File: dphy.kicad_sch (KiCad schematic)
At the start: 5 parts, among them J1901 FFC-22p-P0.5mm, U1901 RCLAMP0524P, U1902 RCLAMP0524P, U1903 RCLAMP0524P, U1904 RCLAMP0524P

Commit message: Add comments about diff pair polarity
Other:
- note added: "DSI diff pair polarity MUST be maintained!"
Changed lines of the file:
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@@
 		(comment 3 "HALPI2 is licensed under CERN-OHL-S v2.")
+	)
+	(text "DSI diff pair polarity\nMUST be maintained!"
+		(exclude_from_sim no)
+		(at 201.676 51.562 0)
+		(effects
+			(font
+				(size 1.27 1.27)
+			)
+			(justify left)
+		)
 	)
 	(junction

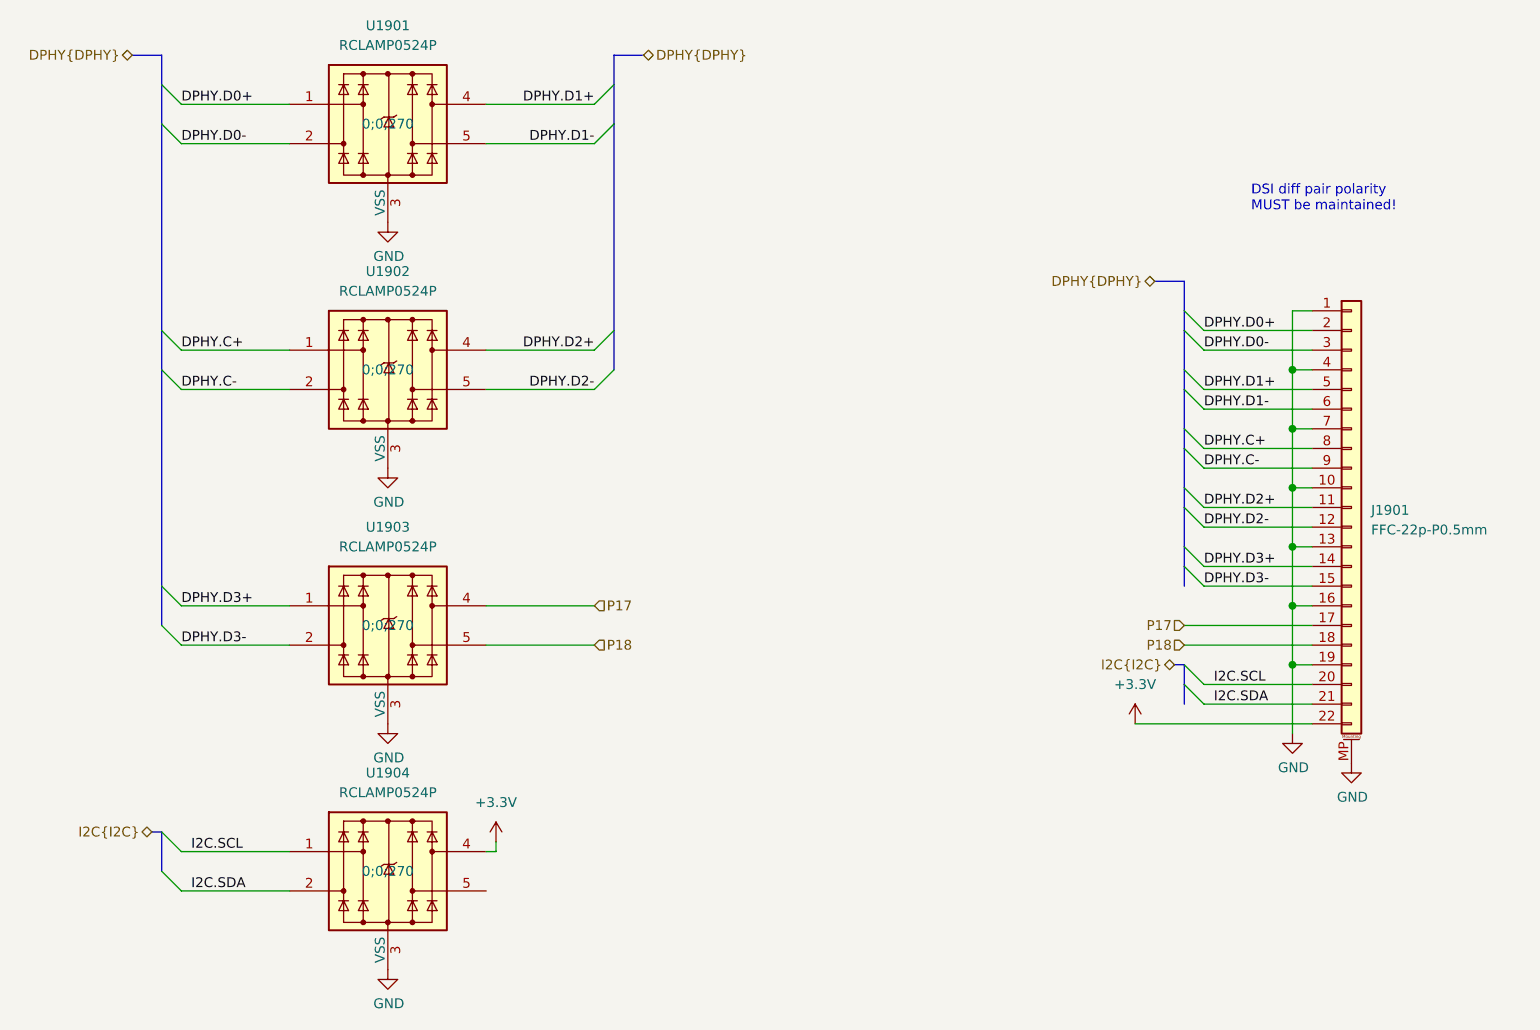
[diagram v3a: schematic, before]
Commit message: Fix DPHY pinout
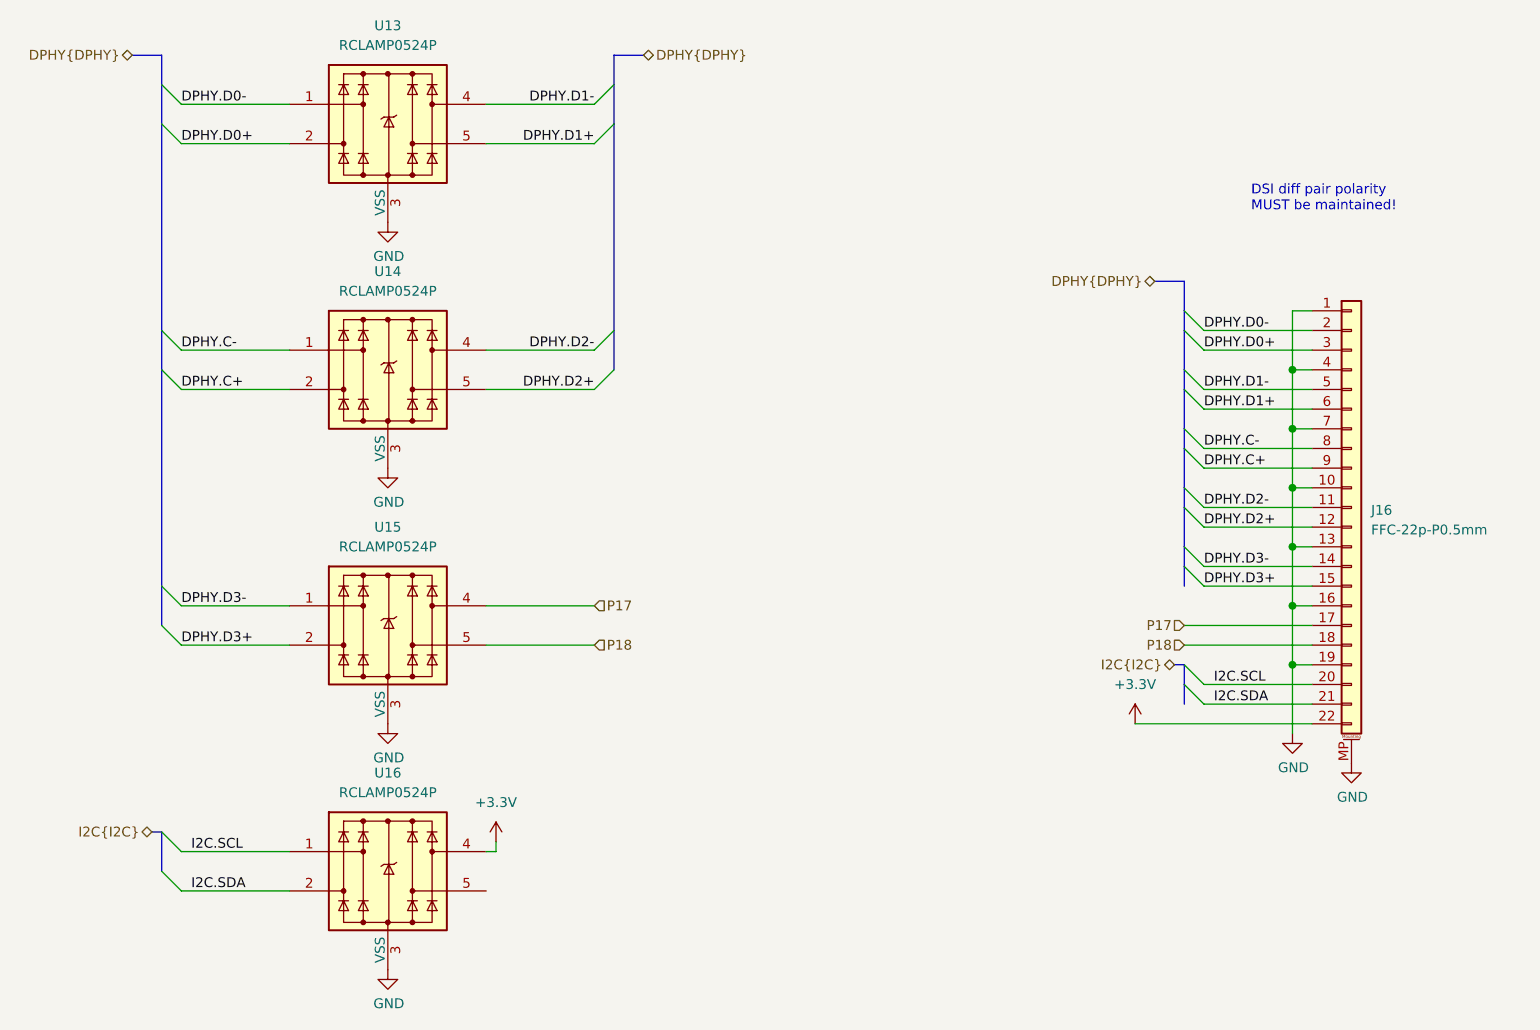
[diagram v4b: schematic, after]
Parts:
- J16: renamed from J1901; footprint Hatlabs:FFC_HDGC_0.5K-A-22PB_1x22-1SV_P0.5mm_Vertical -> HL_Connector:FFC_1x22_JUSHUO_AFC11-S22ICC-00_P0.5mm_Vertical; LCSC C2914146 -> C11074
- renumbered U1901 to U13, U1902 to U14, U1903 to U15, U1904 to U16
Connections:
- net DPHY.C+: now also J16.9 (Pin_9), U14.2, U14.9; no longer J16.8 (Pin_8), U14.1, U14.10
- net DPHY.C-: now also J16.8 (Pin_8), U14.1, U14.10; no longer J16.9 (Pin_9), U14.2, U14.9
- net DPHY.D0+: now also J16.3 (Pin_3), U13.2, U13.9; no longer J16.2 (Pin_2), U13.1, U13.10
- net DPHY.D0-: now also J16.2 (Pin_2), U13.1, U13.10; no longer J16.3 (Pin_3), U13.2, U13.9
- net DPHY.D1+: now also J16.6 (Pin_6), U13.5, U13.6; no longer J16.5 (Pin_5), U13.4, U13.7
- net DPHY.D1-: now also J16.5 (Pin_5), U13.4, U13.7; no longer J16.6 (Pin_6), U13.5, U13.6
- net DPHY.D2+: now also J16.12 (Pin_12), U14.5, U14.6; no longer J16.11 (Pin_11), U14.4, U14.7
- net DPHY.D2-: now also J16.11 (Pin_11), U14.4, U14.7; no longer J16.12 (Pin_12), U14.5, U14.6
- net DPHY.D3+: now also J16.15 (Pin_15), U15.2, U15.9; no longer J16.14 (Pin_14), U15.1, U15.10
- net DPHY.D3-: now also J16.14 (Pin_14), U15.1, U15.10; no longer J16.15 (Pin_15), U15.2, U15.9

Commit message: Reannotate the board
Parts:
- renumbered J16 to J15, U13 to U12, U14 to U13, U15 to U14, U16 to U15
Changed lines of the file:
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@@
 		(on_board yes)
 		(dnp no)
-		(property "Reference" "#PWR0117"
+		(property "Reference" "#PWR0116"
 			(at 207.01 127 0)
 			(effects
@@
 			(project "HALPI2"
 				(path "/abc482bd-3f17-4d35-80db-1da3dcdb5c27/851e7ce4-d5b0-47f7-ace9-4a347f172348/10568cce-38f9-4351-82fd-0cb3bf8ca49d"
-					(reference "#PWR0117")
-					(unit 1)
-				)
-				(path "/abc482bd-3f17-4d35-80db-1da3dcdb5c27/851e7ce4-d5b0-47f7-ace9-4a347f172348/d4876730-9038-4f8b-92bc-bcbb3a62ccf0"
-					(reference "#PWR0125")
+					(reference "#PWR0116")
+					(unit 1)
+				)
+				(path "/abc482bd-3f17-4d35-80db-1da3dcdb5c27/851e7ce4-d5b0-47f7-ace9-4a347f172348/d4876730-9038-4f8b-92bc-bcbb3a62ccf0"
+					(reference "#PWR0124")
 					(unit 1)
 				)
@@
 		(on_board yes)
 		(dnp no)
-		(property "Reference" "#PWR0112"
+		(property "Reference" "#PWR0111"
 			(at 90.17 92.71 0)
 			(effects
@@
 			(project "HALPI2"
 				(path "/abc482bd-3f17-4d35-80db-1da3dcdb5c27/851e7ce4-d5b0-47f7-ace9-4a347f172348/10568cce-38f9-4351-82fd-0cb3bf8ca49d"
-					(reference "#PWR0112")
-					(unit 1)
-				)
-				(path "/abc482bd-3f17-4d35-80db-1da3dcdb5c27/851e7ce4-d5b0-47f7-ace9-4a347f172348/d4876730-9038-4f8b-92bc-bcbb3a62ccf0"
-					(reference "#PWR0120")
+					(reference "#PWR0111")
+					(unit 1)
+				)
+				(path "/abc482bd-3f17-4d35-80db-1da3dcdb5c27/851e7ce4-d5b0-47f7-ace9-4a347f172348/d4876730-9038-4f8b-92bc-bcbb3a62ccf0"
+					(reference "#PWR0119")
 					(unit 1)
 				)
@@
 		(on_board yes)
 		(dnp no)
-		(property "Reference" "#PWR0111"
+		(property "Reference" "#PWR0110"
 			(at 90.17 60.96 0)
 			(effects
@@
 			(project "HALPI2"
 				(path "/abc482bd-3f17-4d35-80db-1da3dcdb5c27/851e7ce4-d5b0-47f7-ace9-4a347f172348/10568cce-38f9-4351-82fd-0cb3bf8ca49d"
-					(reference "#PWR0111")
-					(unit 1)
-				)
-				(path "/abc482bd-3f17-4d35-80db-1da3dcdb5c27/851e7ce4-d5b0-47f7-ace9-4a347f172348/d4876730-9038-4f8b-92bc-bcbb3a62ccf0"
-					(reference "#PWR0119")
+					(reference "#PWR0110")
+					(unit 1)
+				)
+				(path "/abc482bd-3f17-4d35-80db-1da3dcdb5c27/851e7ce4-d5b0-47f7-ace9-4a347f172348/d4876730-9038-4f8b-92bc-bcbb3a62ccf0"
+					(reference "#PWR0118")
 					(unit 1)
 				)
@@
 		(on_board yes)
 		(dnp no)
-		(property "Reference" "U16"
+		(property "Reference" "U15"
 			(at 90.17 125.73 0)
 			(effects
@@
 			(project "HALPI2"
 				(path "/abc482bd-3f17-4d35-80db-1da3dcdb5c27/851e7ce4-d5b0-47f7-ace9-4a347f172348/10568cce-38f9-4351-82fd-0cb3bf8ca49d"
-					(reference "U16")
-					(unit 1)
-				)
-				(path "/abc482bd-3f17-4d35-80db-1da3dcdb5c27/851e7ce4-d5b0-47f7-ace9-4a347f172348/d4876730-9038-4f8b-92bc-bcbb3a62ccf0"
-					(reference "U20")
+					(reference "U15")
+					(unit 1)
+				)
+				(path "/abc482bd-3f17-4d35-80db-1da3dcdb5c27/851e7ce4-d5b0-47f7-ace9-4a347f172348/d4876730-9038-4f8b-92bc-bcbb3a62ccf0"
+					(reference "U19")
 					(unit 1)
 				)
@@
 		(dnp no)
 		(fields_autoplaced yes)
-		(property "Reference" "#PWR0115"
+		(property "Reference" "#PWR0114"
 			(at 104.14 138.43 0)
 			(effects
@@
 			(project "HALPI2"
 				(path "/abc482bd-3f17-4d35-80db-1da3dcdb5c27/851e7ce4-d5b0-47f7-ace9-4a347f172348/10568cce-38f9-4351-82fd-0cb3bf8ca49d"
-					(reference "#PWR0115")
-					(unit 1)
-				)
-				(path "/abc482bd-3f17-4d35-80db-1da3dcdb5c27/851e7ce4-d5b0-47f7-ace9-4a347f172348/d4876730-9038-4f8b-92bc-bcbb3a62ccf0"
-					(reference "#PWR0123")
+					(reference "#PWR0114")
+					(unit 1)
+				)
+				(path "/abc482bd-3f17-4d35-80db-1da3dcdb5c27/851e7ce4-d5b0-47f7-ace9-4a347f172348/d4876730-9038-4f8b-92bc-bcbb3a62ccf0"
+					(reference "#PWR0122")
 					(unit 1)
 				)
@@
 		(on_board yes)
 		(dnp no)
-		(property "Reference" "U14"
+		(property "Reference" "U13"
 			(at 90.17 60.96 0)
 			(effects
@@
 			(project "HALPI2"
 				(path "/abc482bd-3f17-4d35-80db-1da3dcdb5c27/851e7ce4-d5b0-47f7-ace9-4a347f172348/10568cce-38f9-4351-82fd-0cb3bf8ca49d"
-					(reference "U14")
-					(unit 1)
-				)
-				(path "/abc482bd-3f17-4d35-80db-1da3dcdb5c27/851e7ce4-d5b0-47f7-ace9-4a347f172348/d4876730-9038-4f8b-92bc-bcbb3a62ccf0"
-					(reference "U18")
+					(reference "U13")
+					(unit 1)
+				)
+				(path "/abc482bd-3f17-4d35-80db-1da3dcdb5c27/851e7ce4-d5b0-47f7-ace9-4a347f172348/d4876730-9038-4f8b-92bc-bcbb3a62ccf0"
+					(reference "U17")
 					(unit 1)
 				)
@@
 		(on_board yes)
 		(dnp no)
-		(property "Reference" "#PWR0113"
+		(property "Reference" "#PWR0112"
 			(at 90.17 125.73 0)
 			(effects
@@
 			(project "HALPI2"
 				(path "/abc482bd-3f17-4d35-80db-1da3dcdb5c27/851e7ce4-d5b0-47f7-ace9-4a347f172348/10568cce-38f9-4351-82fd-0cb3bf8ca49d"
-					(reference "#PWR0113")
-					(unit 1)
-				)
-				(path "/abc482bd-3f17-4d35-80db-1da3dcdb5c27/851e7ce4-d5b0-47f7-ace9-4a347f172348/d4876730-9038-4f8b-92bc-bcbb3a62ccf0"
-					(reference "#PWR0121")
+					(reference "#PWR0112")
+					(unit 1)
+				)
+				(path "/abc482bd-3f17-4d35-80db-1da3dcdb5c27/851e7ce4-d5b0-47f7-ace9-4a347f172348/d4876730-9038-4f8b-92bc-bcbb3a62ccf0"
+					(reference "#PWR0120")
 					(unit 1)
 				)
@@
 		(on_board yes)
 		(dnp no)
-		(property "Reference" "#PWR0114"
+		(property "Reference" "#PWR0113"
 			(at 90.17 157.48 0)
 			(effects
@@
 			(project "HALPI2"
 				(path "/abc482bd-3f17-4d35-80db-1da3dcdb5c27/851e7ce4-d5b0-47f7-ace9-4a347f172348/10568cce-38f9-4351-82fd-0cb3bf8ca49d"
-					(reference "#PWR0114")
-					(unit 1)
-				)
-				(path "/abc482bd-3f17-4d35-80db-1da3dcdb5c27/851e7ce4-d5b0-47f7-ace9-4a347f172348/d4876730-9038-4f8b-92bc-bcbb3a62ccf0"
-					(reference "#PWR0122")
+					(reference "#PWR0113")
+					(unit 1)
+				)
+				(path "/abc482bd-3f17-4d35-80db-1da3dcdb5c27/851e7ce4-d5b0-47f7-ace9-4a347f172348/d4876730-9038-4f8b-92bc-bcbb3a62ccf0"
+					(reference "#PWR0121")
 					(unit 1)
 				)
@@
 		(on_board yes)
 		(dnp no)
-		(property "Reference" "U13"
+		(property "Reference" "U12"
 			(at 90.17 29.21 0)
 			(effects
@@
 			(project "HALPI2"
 				(path "/abc482bd-3f17-4d35-80db-1da3dcdb5c27/851e7ce4-d5b0-47f7-ace9-4a347f172348/10568cce-38f9-4351-82fd-0cb3bf8ca49d"
-					(reference "U13")
-					(unit 1)
-				)
-				(path "/abc482bd-3f17-4d35-80db-1da3dcdb5c27/851e7ce4-d5b0-47f7-ace9-4a347f172348/d4876730-9038-4f8b-92bc-bcbb3a62ccf0"
-					(reference "U17")
+					(reference "U12")
+					(unit 1)
+				)
+				(path "/abc482bd-3f17-4d35-80db-1da3dcdb5c27/851e7ce4-d5b0-47f7-ace9-4a347f172348/d4876730-9038-4f8b-92bc-bcbb3a62ccf0"
+					(reference "U16")
 					(unit 1)
 				)
@@
 		(on_board yes)
 		(dnp no)
-		(property "Reference" "#PWR0118"
+		(property "Reference" "#PWR0117"
 			(at 214.63 130.81 0)
 			(effects
@@
 			(project "HALPI2"
 				(path "/abc482bd-3f17-4d35-80db-1da3dcdb5c27/851e7ce4-d5b0-47f7-ace9-4a347f172348/10568cce-38f9-4351-82fd-0cb3bf8ca49d"
-					(reference "#PWR0118")
-					(unit 1)
-				)
-				(path "/abc482bd-3f17-4d35-80db-1da3dcdb5c27/851e7ce4-d5b0-47f7-ace9-4a347f172348/d4876730-9038-4f8b-92bc-bcbb3a62ccf0"
-					(reference "#PWR0126")
+					(reference "#PWR0117")
+					(unit 1)
+				)
+				(path "/abc482bd-3f17-4d35-80db-1da3dcdb5c27/851e7ce4-d5b0-47f7-ace9-4a347f172348/d4876730-9038-4f8b-92bc-bcbb3a62ccf0"
+					(reference "#PWR0125")
 					(unit 1)
 				)
@@
 		(dnp no)
 		(fields_autoplaced yes)
-		(property "Reference" "J16"
+		(property "Reference" "J15"
 			(at 217.17 91.7955 0)
 			(effects
@@
 				)
 				(path "/abc482bd-3f17-4d35-80db-1da3dcdb5c27/851e7ce4-d5b0-47f7-ace9-4a347f172348/10568cce-38f9-4351-82fd-0cb3bf8ca49d"
+					(reference "J15")
+					(unit 1)
+				)
+				(path "/abc482bd-3f17-4d35-80db-1da3dcdb5c27/851e7ce4-d5b0-47f7-ace9-4a347f172348/d4876730-9038-4f8b-92bc-bcbb3a62ccf0"
 					(reference "J16")
-					(unit 1)
-				)
-				(path "/abc482bd-3f17-4d35-80db-1da3dcdb5c27/851e7ce4-d5b0-47f7-ace9-4a347f172348/d4876730-9038-4f8b-92bc-bcbb3a62ccf0"
-					(reference "J17")
 					(unit 1)
 				)
@@
 		(on_board yes)
 		(dnp no)
-		(property "Reference" "U15"
+		(property "Reference" "U14"
 			(at 90.17 93.98 0)
 			(effects
@@
 			(project "HALPI2"
 				(path "/abc482bd-3f17-4d35-80db-1da3dcdb5c27/851e7ce4-d5b0-47f7-ace9-4a347f172348/10568cce-38f9-4351-82fd-0cb3bf8ca49d"
-					(reference "U15")
-					(unit 1)
-				)
-				(path "/abc482bd-3f17-4d35-80db-1da3dcdb5c27/851e7ce4-d5b0-47f7-ace9-4a347f172348/d4876730-9038-4f8b-92bc-bcbb3a62ccf0"
-					(reference "U19")
+					(reference "U14")
+					(unit 1)
+				)
+				(path "/abc482bd-3f17-4d35-80db-1da3dcdb5c27/851e7ce4-d5b0-47f7-ace9-4a347f172348/d4876730-9038-4f8b-92bc-bcbb3a62ccf0"
+					(reference "U18")
 					(unit 1)
 				)
@@
 		(dnp no)
 		(fields_autoplaced yes)
-		(property "Reference" "#PWR0116"
+		(property "Reference" "#PWR0115"
 			(at 186.69 123.19 0)
 			(effects
@@
 			(project ""
 				(path "/abc482bd-3f17-4d35-80db-1da3dcdb5c27/851e7ce4-d5b0-47f7-ace9-4a347f172348/10568cce-38f9-4351-82fd-0cb3bf8ca49d"
-					(reference "#PWR0116")
-					(unit 1)
-				)
-				(path "/abc482bd-3f17-4d35-80db-1da3dcdb5c27/851e7ce4-d5b0-47f7-ace9-4a347f172348/d4876730-9038-4f8b-92bc-bcbb3a62ccf0"
-					(reference "#PWR0124")
-					(unit 1)
-				)
+					(reference "#PWR0115")
+					(unit 1)
+				)
+				(path "/abc482bd-3f17-4d35-80db-1da3dcdb5c27/851e7ce4-d5b0-47f7-ace9-4a347f172348/d4876730-9038-4f8b-92bc-bcbb3a62ccf0"
+					(reference "#PWR0123")
+					(unit 1)
+				)
